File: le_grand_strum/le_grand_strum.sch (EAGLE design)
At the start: 101 parts, among them IC1 REG1117, IC2 PIC16F1825SO14, IC3 74HC595D, IC4 74HC595D, SW1 12MMTACT_SMT, SW10 12MMTACT_SMT, SW11 12MMTACT_SMT, SW12 12MMTACT_SMT, SW13 12MMTACT_SMT, SW14 12MMTACT_SMT, SW15 12MMTACT_SMT, SW16 12MMTACT_SMT, SW17 12MMTACT_SMT, SW18 12MMTACT_SMT, SW19 12MMTACT_SMT, SW2 12MMTACT_SMT, SW20 12MMTACT_SMT, SW21 12MMTACT_SMT, SW22 12MMTACT_SMT, SW23 12MMTACT_SMT, SW24 12MMTACT_SMT, SW25 12MMTACT_SMT, SW26 12MMTACT_SMT, SW27 12MMTACT_SMT, SW28 12MMTACT_SMT, SW29 12MMTACT_SMT, SW3 12MMTACT_SMT, SW30 12MMTACT_SMT, SW31 12MMTACT_SMT, SW32 12MMTACT_SMT, SW33 12MMTACT_SMT, SW34 12MMTACT_SMT, SW35 12MMTACT_SMT, SW36 12MMTACT_SMT, SW4 12MMTACT_SMT, SW5 12MMTACT_SMT, SW6 12MMTACT_SMT, SW7 12MMTACT_SMT, SW8 12MMTACT_SMT, SW9 12MMTACT_SMT

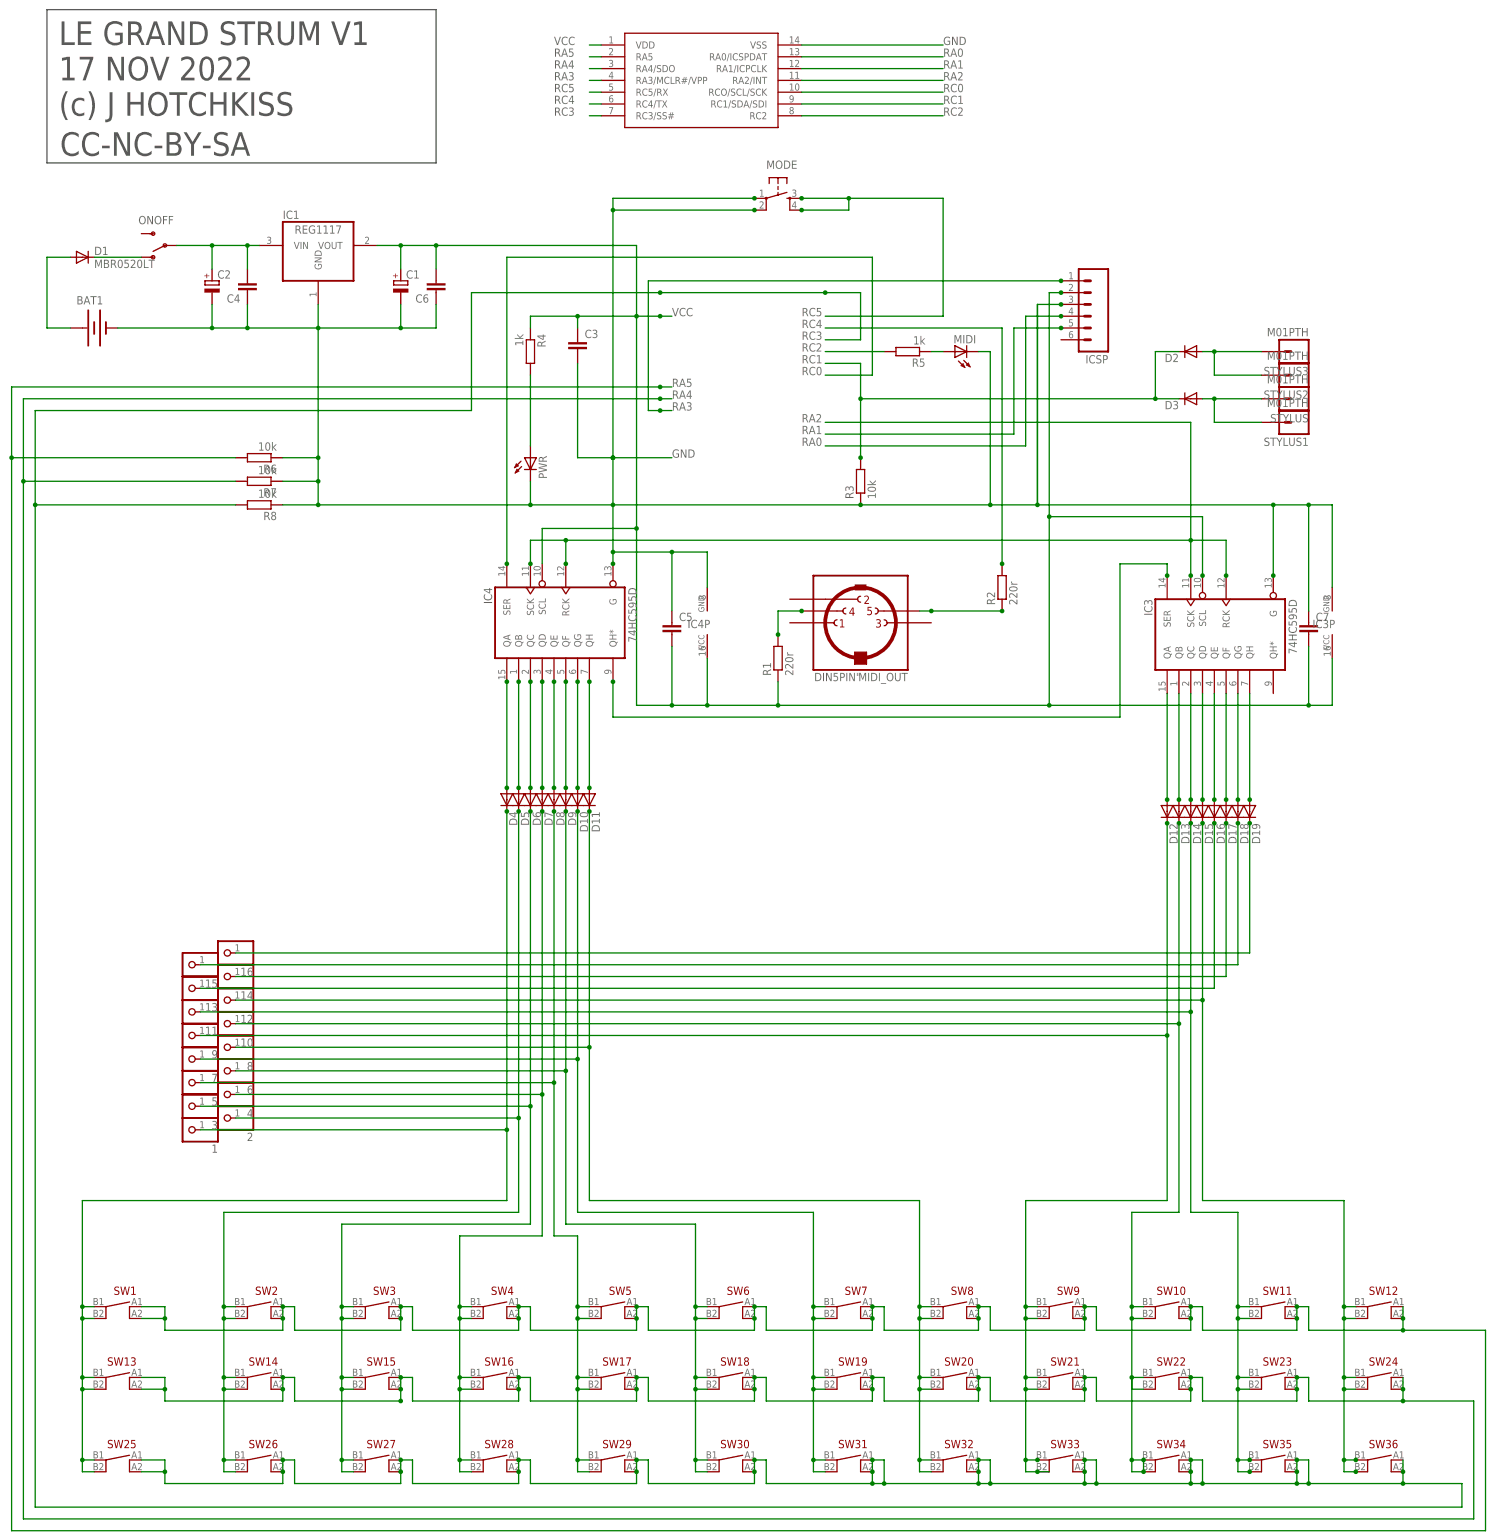
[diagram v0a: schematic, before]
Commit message: rev2 board thru hole switches
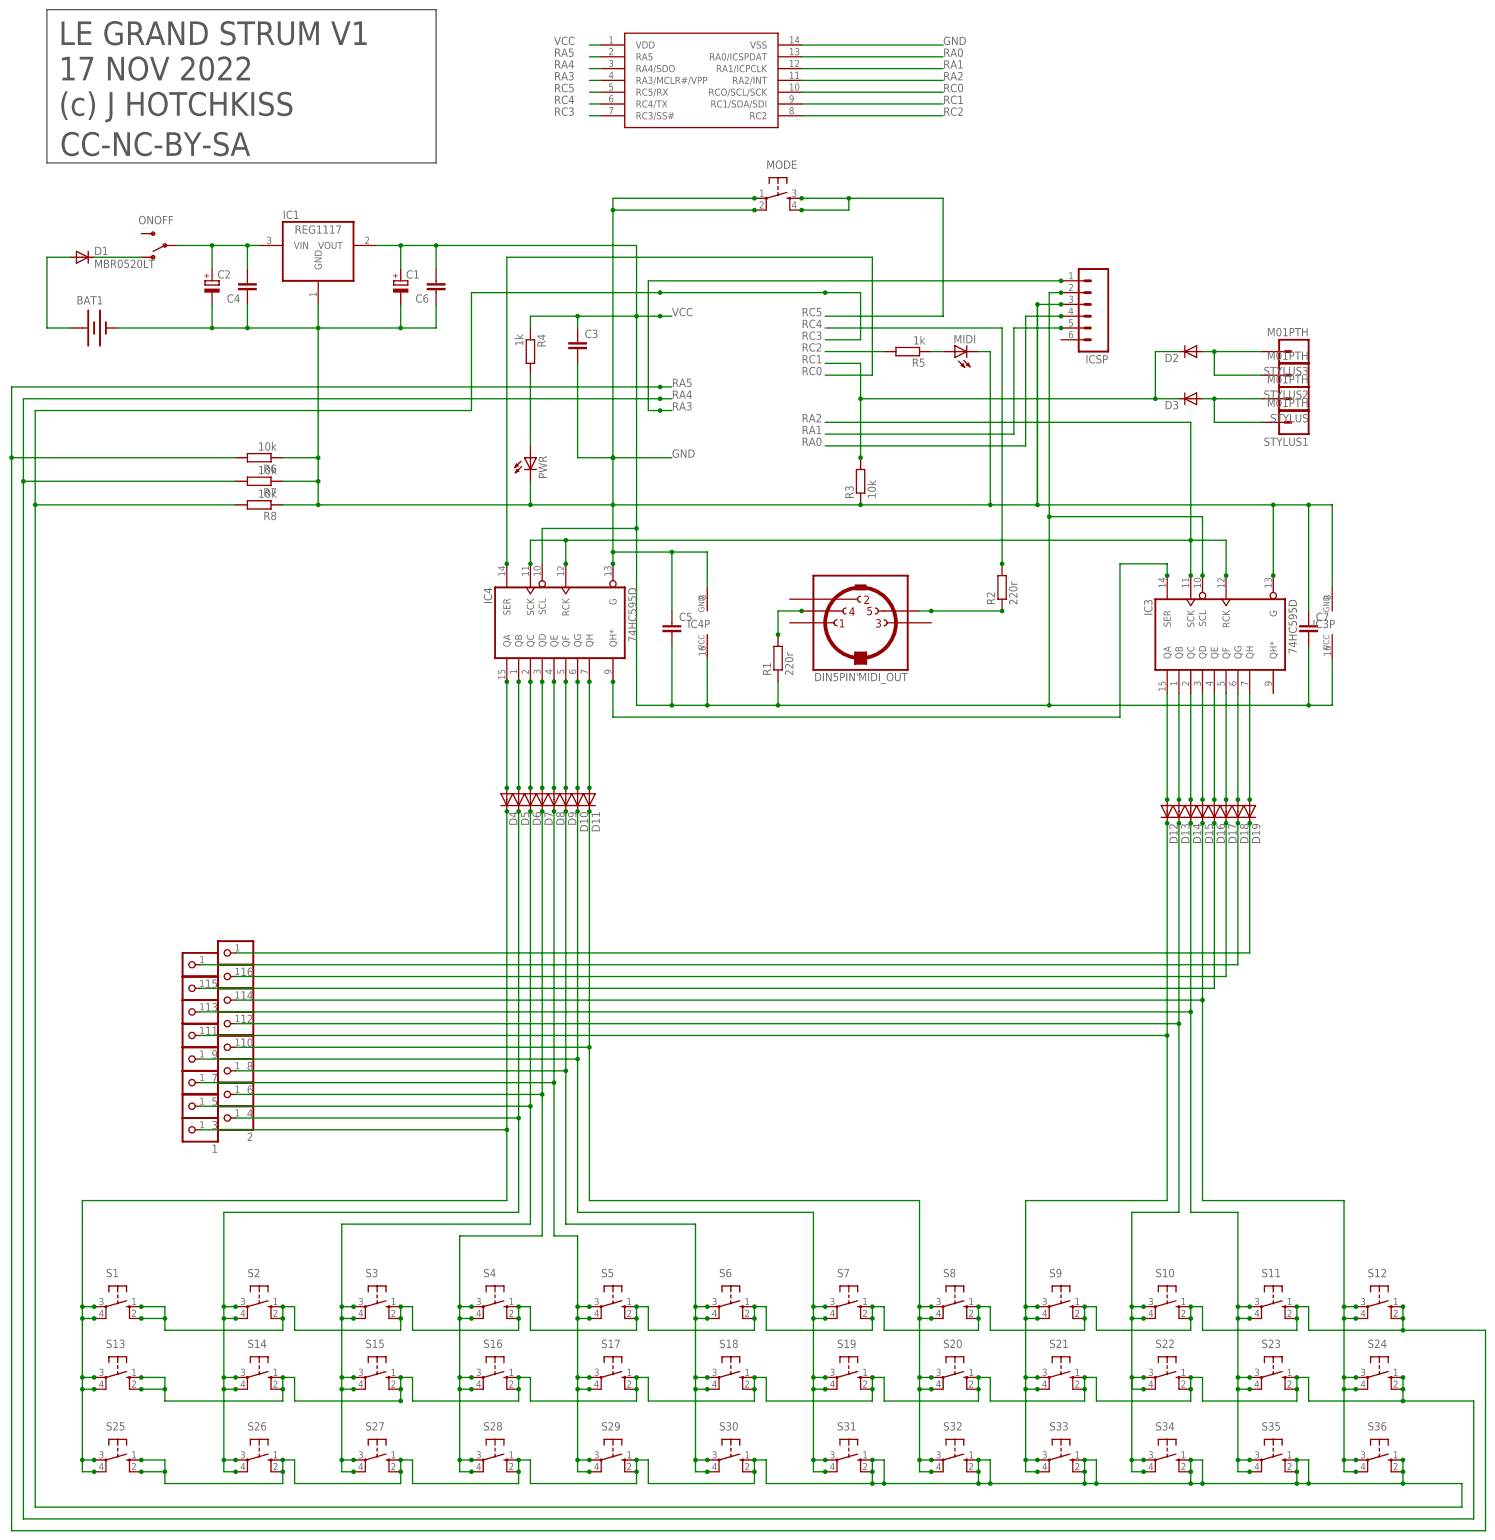
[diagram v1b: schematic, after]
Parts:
- removed SW1, SW10, SW11, SW12, SW13, SW14, SW15, SW16, SW17, SW18, SW19, SW2, SW20, SW21, SW22, SW23, SW24, SW25, SW26, SW27, SW28, SW29, SW3, SW30, SW31, SW32, SW33, SW34, SW35, SW36, SW4, SW5, SW6, SW7, SW8, SW9: 12MMTACT_SMT, jason_eagle6:12MMTACT_SMT
- added S1, S10, S11, S12, S13, S14, S15, S16, S17, S18, S19, S2, S20, S21, S22, S23, S24, S25, S26, S27, S28, S29, S3, S30, S31, S32, S33, S34, S35, S36, S4, S5, S6, S7, S8, S9: (no value), switch-omron:40-XX
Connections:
- net LINE1: now also S1.P, S1.P1, S13.P, S13.P1, S25.P, S25.P1; no longer SW1.3, SW1.4, SW13.3, SW13.4, SW25.3, SW25.4
- net LINE10: now also S10.P, S10.P1, S22.P, S22.P1, S34.P, S34.P1; no longer SW10.3, SW10.4, SW22.3, SW22.4, SW34.3, SW34.4
- net LINE11: now also S11.P, S11.P1, S23.P, S23.P1, S35.P, S35.P1; no longer SW11.3, SW11.4, SW23.3, SW23.4, SW35.3, SW35.4
- net LINE12: now also S12.P, S12.P1, S24.P, S24.P1, S36.P, S36.P1; no longer SW12.3, SW12.4, SW24.3, SW24.4, SW36.3, SW36.4
- net LINE2: now also S14.P, S14.P1, S2.P, S2.P1, S26.P, S26.P1; no longer SW14.3, SW14.4, SW2.3, SW2.4, SW26.3, SW26.4
- net LINE3: now also S15.P, S15.P1, S27.P, S27.P1, S3.P, S3.P1; no longer SW15.3, SW15.4, SW27.3, SW27.4, SW3.3, SW3.4
- net LINE4: now also S16.P, S16.P1, S28.P, S28.P1, S4.P, S4.P1; no longer SW16.3, SW16.4, SW28.3, SW28.4, SW4.3, SW4.4
- net LINE5: now also S17.P, S17.P1, S29.P, S29.P1, S5.P, S5.P1; no longer SW17.3, SW17.4, SW29.3, SW29.4, SW5.3, SW5.4
- net LINE6: now also S18.P, S18.P1, S30.P, S30.P1, S6.P, S6.P1; no longer SW18.3, SW18.4, SW30.3, SW30.4, SW6.3, SW6.4
- net LINE7: now also S19.P, S19.P1, S31.P, S31.P1, S7.P, S7.P1; no longer SW19.3, SW19.4, SW31.3, SW31.4, SW7.3, SW7.4
- net LINE8: now also S20.P, S20.P1, S32.P, S32.P1, S8.P, S8.P1; no longer SW20.3, SW20.4, SW32.3, SW32.4, SW8.3, SW8.4
- net LINE9: now also S21.P, S21.P1, S33.P, S33.P1, S9.P, S9.P1; no longer SW21.3, SW21.4, SW33.3, SW33.4, SW9.3, SW9.4
- net RA4: now also S13.S, S13.S1, S14.S, S14.S1, S15.S, S15.S1, S16.S, S16.S1, S17.S, S17.S1, S18.S, S18.S1, S19.S, S19.S1, S20.S, S20.S1, S21.S, S21.S1, S22.S, S22.S1, S23.S, S23.S1, S24.S, S24.S1; no longer SW13.1, SW13.2, SW14.1, SW14.2, SW15.1, SW15.2, SW16.1, SW16.2, SW17.1, SW17.2, SW18.1, SW18.2, SW19.1, SW19.2, SW20.1, SW20.2, SW21.1, SW21.2, SW22.1, SW22.2, SW23.1, SW23.2, SW24.1, SW24.2
- net RA5: now also S1.S, S1.S1, S10.S, S10.S1, S11.S, S11.S1, S12.S, S12.S1, S2.S, S2.S1, S3.S, S3.S1, S4.S, S4.S1, S5.S, S5.S1, S6.S, S6.S1, S7.S, S7.S1, S8.S, S8.S1, S9.S, S9.S1; no longer SW1.1, SW1.2, SW10.1, SW10.2, SW11.1, SW11.2, SW12.1, SW12.2, SW2.1, SW2.2, SW3.1, SW3.2, SW4.1, SW4.2, SW5.1, SW5.2, SW6.1, SW6.2, SW7.1, SW7.2, SW8.1, SW8.2, SW9.1, SW9.2
- net RC3: now also S25.S, S25.S1, S26.S, S26.S1, S27.S, S27.S1, S28.S, S28.S1, S29.S, S29.S1, S30.S, S30.S1, S31.S, S31.S1, S32.S, S32.S1, S33.S, S33.S1, S34.S, S34.S1, S35.S, S35.S1, S36.S, S36.S1; no longer SW25.1, SW25.2, SW26.1, SW26.2, SW27.1, SW27.2, SW28.1, SW28.2, SW29.1, SW29.2, SW30.1, SW30.2, SW31.1, SW31.2, SW32.1, SW32.2, SW33.1, SW33.2, SW34.1, SW34.2, SW35.1, SW35.2, SW36.1, SW36.2

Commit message: VERSION 3
ground midi out pin 2
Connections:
- net GND: now also MIDI_OUT.2
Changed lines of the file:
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@@
 <wire x1="261.62" y1="340.36" x2="261.62" y2="342.9" width="0.1524" layer="91"/>
 <wire x1="261.62" y1="342.9" x2="261.62" y2="353.06" width="0.1524" layer="91"/>
-<wire x1="261.62" y1="353.06" x2="314.96" y2="353.06" width="0.1524" layer="91"/>
+<wire x1="261.62" y1="353.06" x2="297.18" y2="353.06" width="0.1524" layer="91"/>
+<wire x1="297.18" y1="353.06" x2="314.96" y2="353.06" width="0.1524" layer="91"/>
 <wire x1="353.06" y1="353.06" x2="403.86" y2="353.06" width="0.1524" layer="91"/>
 <wire x1="403.86" y1="353.06" x2="411.48" y2="353.06" width="0.1524" layer="91"/>
@@
 <wire x1="261.62" y1="363.22" x2="274.32" y2="363.22" width="0.1524" layer="91"/>
 <wire x1="358.14" y1="396.24" x2="353.06" y2="396.24" width="0.1524" layer="91"/>
-<wire x1="353.06" y1="396.24" x2="353.06" y2="353.06" width="0.1524" layer="91"/>
 <wire x1="261.62" y1="353.06" x2="243.84" y2="353.06" width="0.1524" layer="91"/>
 <wire x1="243.84" y1="353.06" x2="198.12" y2="353.06" width="0.1524" layer="91"/>
@@
 <wire x1="353.06" y1="396.24" x2="353.06" y2="353.06" width="0.1524" layer="91"/>
 <junction x="353.06" y="396.24"/>
+<pinref part="MIDI_OUT" gate="G$1" pin="2"/>
+<wire x1="299.72" y1="332.74" x2="297.18" y2="332.74" width="0.1524" layer="91"/>
+<wire x1="297.18" y1="332.74" x2="297.18" y2="353.06" width="0.1524" layer="91"/>
+<junction x="297.18" y="353.06"/>
 </segment>
 <segment>
